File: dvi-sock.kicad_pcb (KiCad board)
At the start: 2 copper layers, 25.2 x 22.5 mm, 15 parts, among them J1 Conn_01x05, J2 Conn_01x05, J3 Conn_01x03, J4 NOT_HDMI_A, J5 2.54mm_2p_nofit

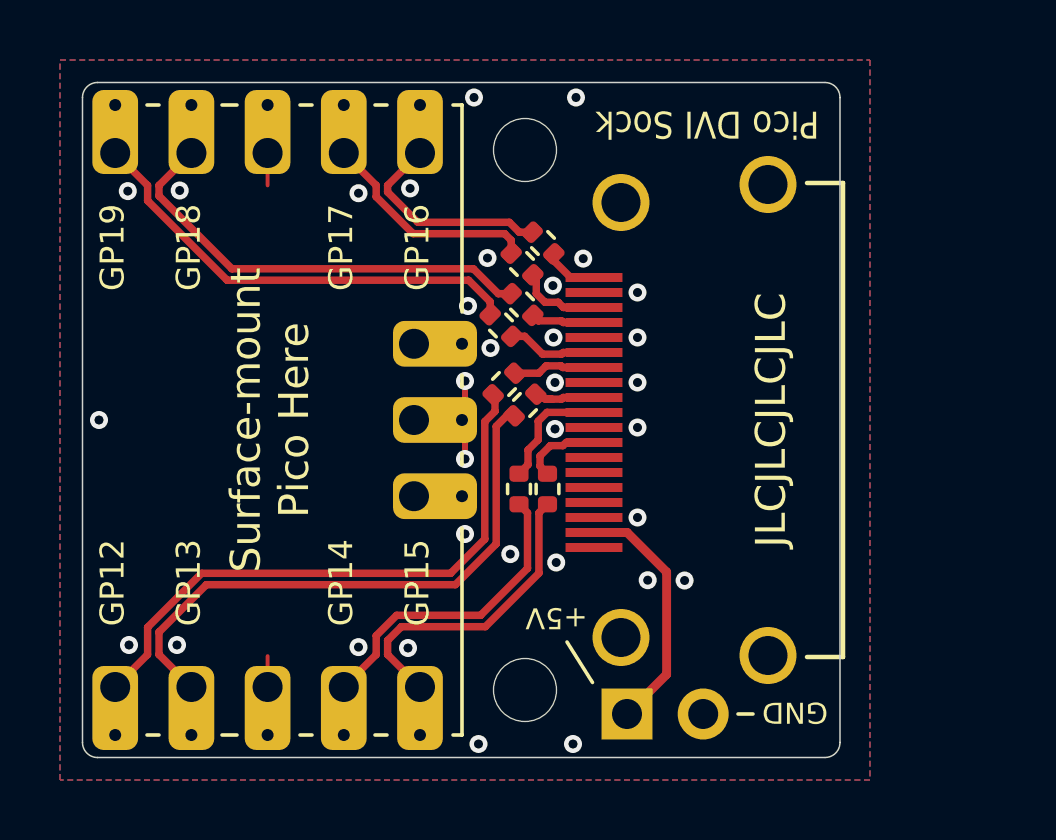
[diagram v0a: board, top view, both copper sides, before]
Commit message: Rev B: Use parts available for JLCPCB SMT assembly
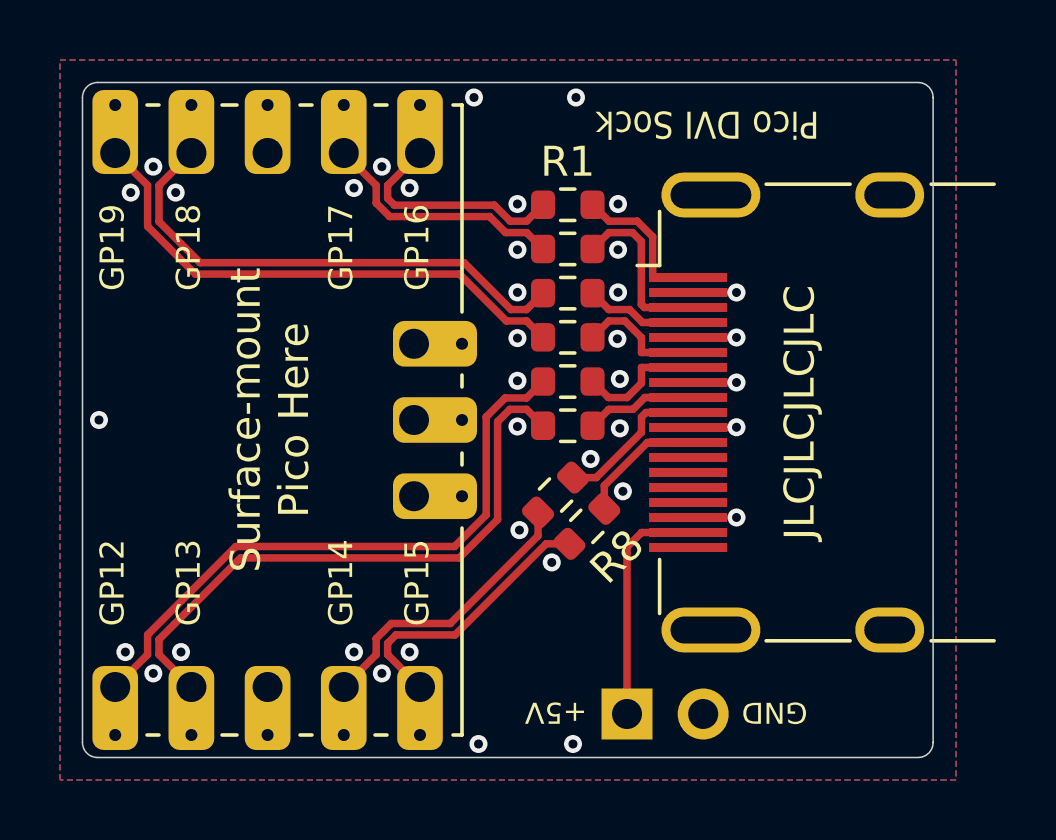
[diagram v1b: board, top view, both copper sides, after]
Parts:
- removed REF** (x2): MH_Pico_M2ish, dvi-sock:MH_Pico_M2ish
- J4: footprint dvi-sock:HDMI-SS-53000 -> Connector_HDMI:HDMI_A_Molex_208658-1001_Horizontal
- R1, R2, R3, R4, R5, R6, R7, R8: footprint Resistor_SMD:R_0402_1005Metric -> Resistor_SMD:R_0603_1608Metric
- moved J4 5.53 mm to (165.2, 84.8), turned to 0 degrees
- moved R4 2.26 mm to (157.9, 82.2), turned to 180 degrees
- moved R5 2.13 mm to (157.9, 83.7), turned to 0 degrees
- moved R8 1.81 mm to (158.6, 88.5), turned to -135 degrees
- moved R2 1.61 mm to (157.9, 79.3), turned to 180 degrees
- moved R6 1.58 mm to (157.9, 85.2), turned to 180 degrees
- moved R3 1.57 mm to (157.9, 80.8), turned to 0 degrees
- moved R1 1.52 mm to (157.9, 77.8), turned to 0 degrees
- moved R7 1.24 mm to (157.5, 87.5), turned to 45 degrees
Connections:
- R2 pad 1: /PICO_D2- -> /D2-
- R2 pad 2: /D2- -> /PICO_D2-
- R4 pad 1: /PICO_D1- -> /D1-
- R4 pad 2: /D1- -> /PICO_D1-
- R6 pad 1: /PICO_D0- -> /D0-
- R6 pad 2: /D0- -> /PICO_D0-
- R8 pad 1: /PICO_CK- -> /CK-
- R8 pad 2: /CK- -> /PICO_CK-
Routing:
- net /D2+: track 1.80 -> 4.99 mm
- net /D2-: track 2.99 -> 5.68 mm
- net /PICO_D1-: track 15.3 -> 17.6 mm
- net /PICO_D1+: track 15.0 -> 17.0 mm
- net GND: track 4.79 -> 6.46 mm, vias 33 -> 38
- net /CK-: track 2.68 -> 4.16 mm
- net /D1+: track 2.14 -> 3.59 mm
- net /D0+: track 2.76 -> 4.13 mm
- net /D0-: track 2.24 -> 3.58 mm
- net /PICO_CK-: track 10.6 -> 9.33 mm
- net /D1-: track 3.01 -> 4.14 mm
- net /CK+: track 4.00 -> 5.03 mm
- net /PICO_D0+: track 19.9 -> 20.8 mm
- net /PICO_D2-: track 7.44 -> 8.31 mm
- net /PICO_D0-: track 19.4 -> 20.1 mm
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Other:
- board size 25.2 x 22.5 mm -> 28.4 x 22.5 mm
- board text added: "Rev B"
- board text removed: "Rev A"
